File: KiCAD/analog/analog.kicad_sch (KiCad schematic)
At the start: 0 parts

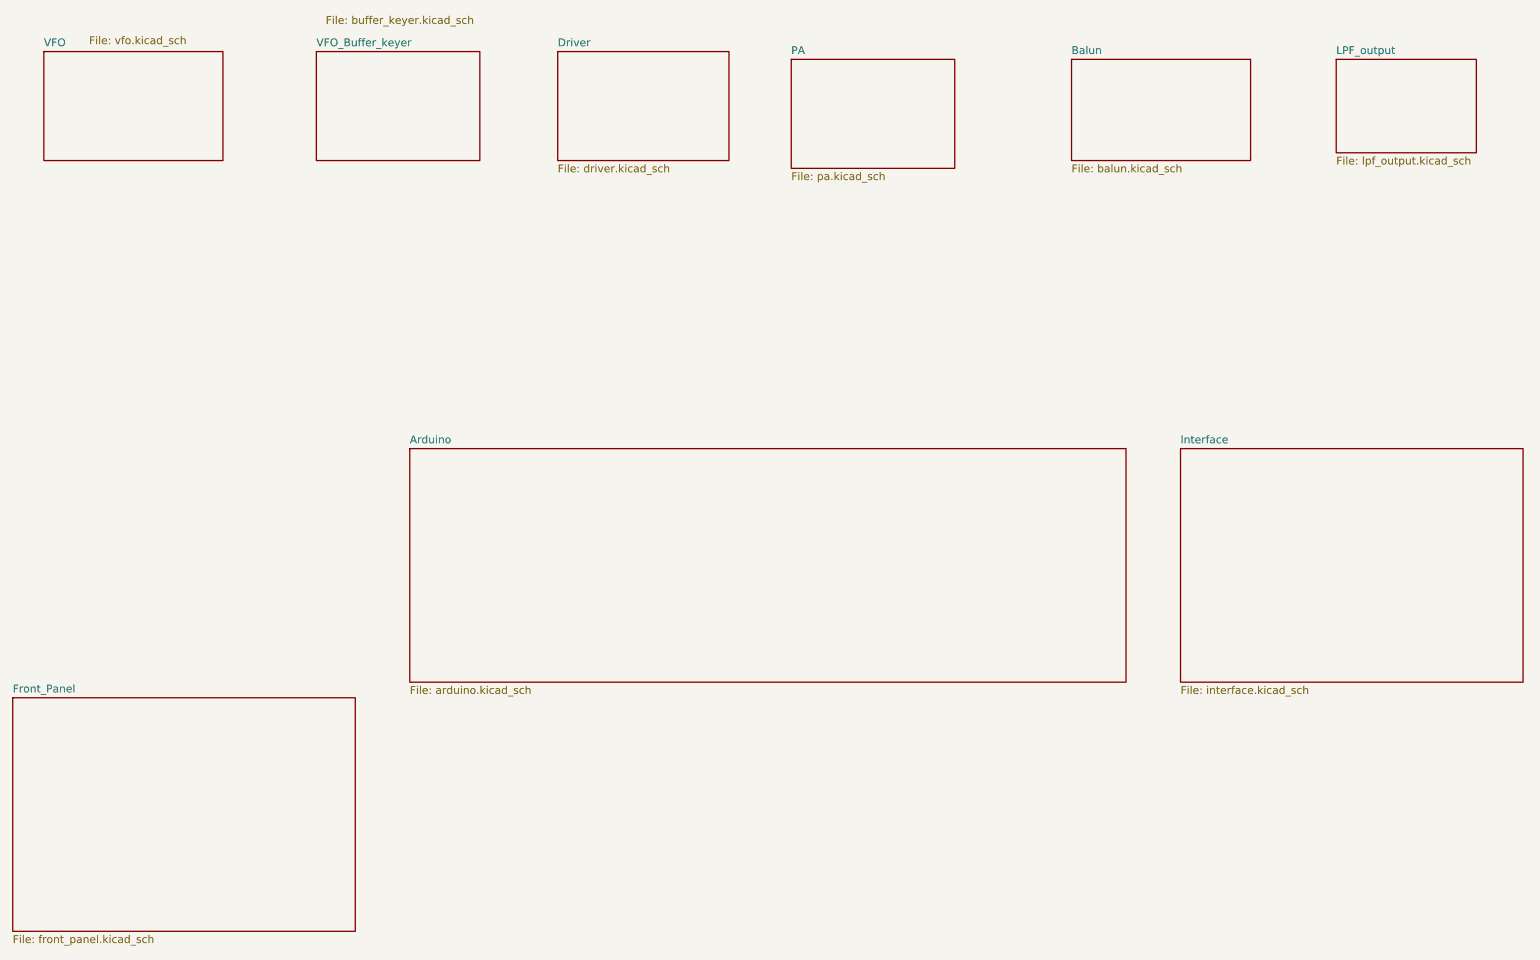
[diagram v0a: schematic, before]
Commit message: Drop empty stubs (PA/Driver/Balun/LPF_output/Front_Panel) from analog
None of these contributed components, nets, or PCB footprints on Rev A;
they were placeholder sub-sheets for future work. PA/Driver/Balun/
LPF_output will come back when the RF-chain board project is created
(a separate KiCAD/rf/ project, not part of analog). Front_Panel notes
were preserved by copying the text block into KiCAD/frontpanel/
frontpanel.kicad_sch first — the new frontpanel project is the actual
front-panel PCB.

Removed from analog.kicad_sch: five (sheet ...) blocks.
Removed from analog.kicad_pro: five UUID entries in the "sheets" list.
Deleted files: driver/pa/balun/lpf_output/front_panel.kicad_sch.

Rev A gerbers unaffected (fabricated 2026-07-14, byte-identical copy
preserved at KiCAD/analog/gerber/).

Co-Authored-By: Claude Opus 4.7 <noreply@anthropic.com>
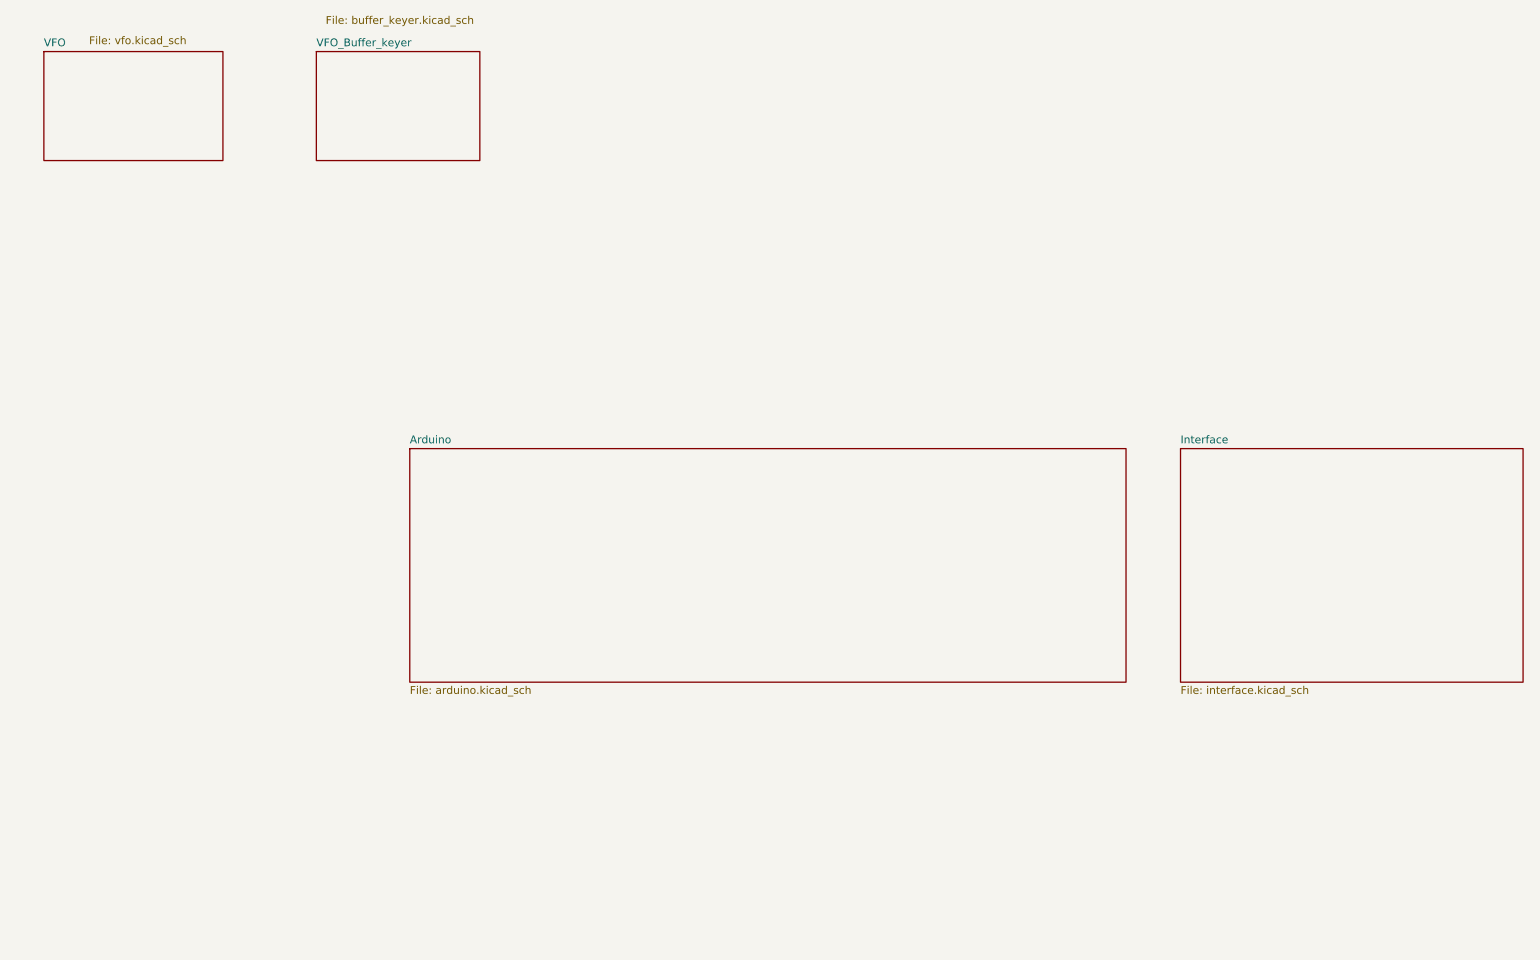
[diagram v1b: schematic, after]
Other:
- removed sheet Balun
- removed sheet Driver
- removed sheet Front_Panel
- removed sheet LPF_output
- removed sheet PA
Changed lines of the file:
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@@
-	)
-	(sheet
-		(at 241.3 43.18)
-		(size 22.86 15.24)
-		(exclude_from_sim no)
-		(in_bom yes)
-		(on_board yes)
-		(dnp no)
-		(fields_autoplaced yes)
-		(stroke
-			(width 0.1524)
-			(type solid)
-		)
-		(fill
-			(color 0 0 0 0)
-		)
-		(property "Sheetname" "LPF_output"
-			(at 241.3 42.4684 0)
-			(show_name no)
-			(do_not_autoplace no)
-			(effects
-				(font
-					(size 1.27 1.27)
-				)
-				(justify left bottom)
-			)
-		)
-		(property "Sheetfile" "lpf_output.kicad_sch"
-			(at 241.3 59.0046 0)
-			(show_name no)
-			(do_not_autoplace no)
-			(effects
-				(font
-					(size 1.27 1.27)
-				)
-				(justify left top)
-			)
-		)
-		(instances
-			(project "KiCAD"
-				(path "/d3de40b8-856b-4fbd-829c-f45ffcd55742"
-					(page "8")
-				)
-			)
-		)
-	)
-	(sheet
-		(at 114.3 41.91)
-		(size 27.94 17.78)
-		(exclude_from_sim no)
-		(in_bom yes)
-		(on_board yes)
-		(dnp no)
-		(fields_autoplaced yes)
-		(stroke
-			(width 0.1524)
-			(type solid)
-		)
-		(fill
-			(color 0 0 0 0)
-		)
-		(property "Sheetname" "Driver"
-			(at 114.3 41.1984 0)
-			(show_name no)
-			(do_not_autoplace no)
-			(effects
-				(font
-					(size 1.27 1.27)
-				)
-				(justify left bottom)
-			)
-		)
-		(property "Sheetfile" "driver.kicad_sch"
-			(at 114.3 60.2746 0)
-			(show_name no)
-			(do_not_autoplace no)
-			(effects
-				(font
-					(size 1.27 1.27)
-				)
-				(justify left top)
-			)
-		)
-		(instances
-			(project "KiCAD"
-				(path "/d3de40b8-856b-4fbd-829c-f45ffcd55742"
-					(page "5")
-				)
-			)
-		)
 	)
 	(sheet
@@
 				(path "/d3de40b8-856b-4fbd-829c-f45ffcd55742"
 					(page "10")
-				)
-			)
-		)
-	)
-	(sheet
-		(at 25.4 147.32)
-		(size 55.88 38.1)
-		(exclude_from_sim no)
-		(in_bom yes)
-		(on_board yes)
-		(dnp no)
-		(fields_autoplaced yes)
-		(stroke
-			(width 0.1524)
-			(type solid)
-		)
-		(fill
-			(color 0 0 0 0)
-		)
-		(property "Sheetname" "Front_Panel"
-			(at 25.4 146.6084 0)
-			(show_name no)
-			(do_not_autoplace no)
-			(effects
-				(font
-					(size 1.27 1.27)
-				)
-				(justify left bottom)
-			)
-		)
-		(property "Sheetfile" "front_panel.kicad_sch"
-			(at 25.4 186.0046 0)
-			(show_name no)
-			(do_not_autoplace no)
-			(effects
-				(font
-					(size 1.27 1.27)
-				)
-				(justify left top)
-			)
-		)
-		(instances
-			(project "KiCAD"
-				(path "/d3de40b8-856b-4fbd-829c-f45ffcd55742"
-					(page "11")
-				)
-			)
-		)
-	)
-	(sheet
-		(at 198.12 43.18)
-		(size 29.21 16.51)
-		(exclude_from_sim no)
-		(in_bom yes)
-		(on_board yes)
-		(dnp no)
-		(fields_autoplaced yes)
-		(stroke
-			(width 0.1524)
-			(type solid)
-		)
-		(fill
-			(color 0 0 0 0)
-		)
-		(property "Sheetname" "Balun"
-			(at 198.12 42.4684 0)
-			(show_name no)
-			(do_not_autoplace no)
-			(effects
-				(font
-					(size 1.27 1.27)
-				)
-				(justify left bottom)
-			)
-		)
-		(property "Sheetfile" "balun.kicad_sch"
-			(at 198.12 60.2746 0)
-			(show_name no)
-			(do_not_autoplace no)
-			(effects
-				(font
-					(size 1.27 1.27)
-				)
-				(justify left top)
-			)
-		)
-		(instances
-			(project "KiCAD"
-				(path "/d3de40b8-856b-4fbd-829c-f45ffcd55742"
-					(page "7")
 				)
 			)
@@
 				)
 			)
-		)
-	)
-	(sheet
-		(at 152.4 43.18)
-		(size 26.67 17.78)
-		(exclude_from_sim no)
-		(in_bom yes)
-		(on_board yes)
-		(dnp no)
-		(fields_autoplaced yes)
-		(stroke
-			(width 0.1524)
-			(type solid)
-		)
-		(fill
-			(color 0 0 0 0)
-		)
-		(property "Sheetname" "PA"
-			(at 152.4 42.4684 0)
-			(show_name no)
-			(do_not_autoplace no)
-			(effects
-				(font
-					(size 1.27 1.27)
-				)
-				(justify left bottom)
-			)
-		)
-		(property "Sheetfile" "pa.kicad_sch"
-			(at 152.4 61.5446 0)
-			(show_name no)
-			(do_not_autoplace no)
-			(effects
-				(font
-					(size 1.27 1.27)
-				)
-				(justify left top)
-			)
-		)
-		(instances
-			(project "KiCAD"
-				(path "/d3de40b8-856b-4fbd-829c-f45ffcd55742"
-					(page "6")
-				)
-			)

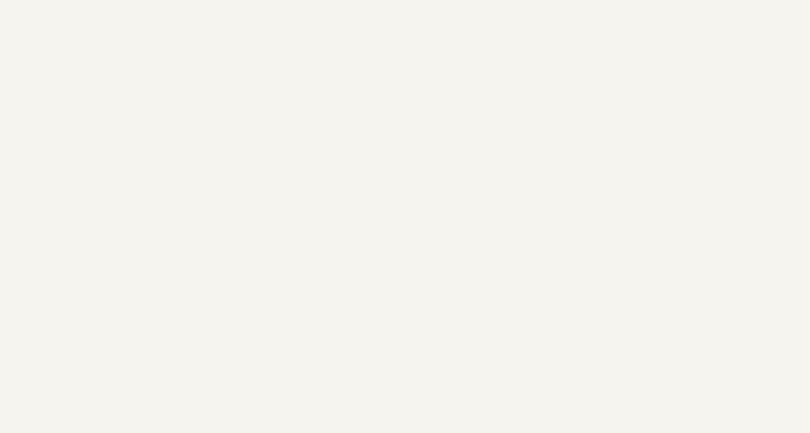
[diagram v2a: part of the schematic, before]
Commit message: KiCad revB: RCA40673 grid fix, VFO_Complete sheet, interface pin fix
- xmitter.kicad_sym: move RCA40673 G1/G2 pins to ±1.27 mm, D/S to
  ±3.81 mm so all four pin tips land on the 50-mil grid and accept
  horizontal wires without snapping issues
- analog.kicad_sch + .kicad_pro: add VFO_Complete (untitled.kicad_sch)
  as page 5 of the hierarchy; update used_designators
- interface.kicad_sch: swap AM26LS32ACN channels 1 and 4 so 1B/1Y and
  4B/4Y pin numbers and directions are correctly ordered in the embedded
  symbol copy
- untitled.kicad_sch: new DGFET keyer schematic sheet (RCA40673 Si5351
  drive chain, Gate-2 envelope control stub)
- Documentation/Components/: add 40673-curves.pdf and
  RCA-Linear-Integrated-Circuits-1977.pdf datasheets
- xmitter_prj/vfo_complete.sch: QUCS-S VFO complete schematic

Co-Authored-By: Claude Sonnet 4.6 <noreply@anthropic.com>
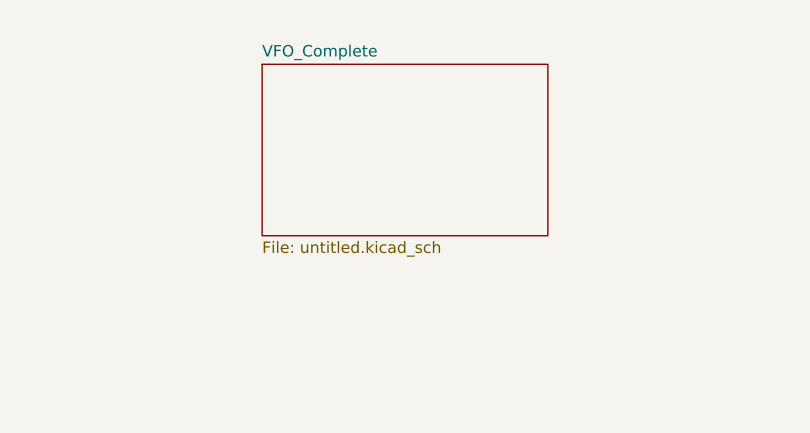
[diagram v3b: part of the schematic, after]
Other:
- added sheet VFO_Complete (untitled.kicad_sch)
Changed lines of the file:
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@@
+	)
+	(sheet
+		(at 138.43 40.64)
+		(size 31.75 19.05)
+		(exclude_from_sim no)
+		(in_bom yes)
+		(on_board yes)
+		(dnp no)
+		(fields_autoplaced yes)
+		(stroke
+			(width 0.1524)
+			(type solid)
+		)
+		(fill
+			(color 0 0 0 0)
+		)
+		(property "Sheetname" "VFO_Complete"
+			(at 138.43 39.9284 0)
+			(show_name no)
+			(do_not_autoplace no)
+			(effects
+				(font
+					(size 1.27 1.27)
+				)
+				(justify left bottom)
+			)
+		)
+		(property "Sheetfile" "untitled.kicad_sch"
+			(at 138.43 60.2746 0)
+			(show_name no)
+			(do_not_autoplace no)
+			(effects
+				(font
+					(size 1.27 1.27)
+				)
+				(justify left top)
+			)
+		)
+		(instances
+			(project "analog"
+				(path "/d3de40b8-856b-4fbd-829c-f45ffcd55742"
+					(page "5")
+				)
+			)
+		)
 	)
 	(sheet
